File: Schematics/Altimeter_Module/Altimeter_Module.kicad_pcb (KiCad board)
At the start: 4 copper layers, 69.5 x 60 mm, 106 parts, among them J1 Stack Male Edge Connector, J2 Main E-Match, J3 Drogue E-Match, J4 USB_C_Female_USB2_Small, J5 SWD_01x04_Pin, Q1 AO3400A, Q2 AO4406AL, Q3 AO3400A, Q4 AO3400A, Q5 AO4406AL, SW1 SW_STM_RESET, SW2 SW_STM_BOOT_MODE, U1 KX134-1211, U10 ACS70331EOLC, U12 AMS1117-3.3, U2 MS560702BA03-50, U3 W25Q128JVS, U4 LM66100DCKR, U5 LM66100DCKR, U6 STM32F103CBT6, U7 LM66100DCKR, U8 ISO1042BDWVR, U9 MPU-6050, Y1 X322516MMB4SI

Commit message: Design version bump to V1.1
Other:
- board text added: "Oka Rev 1.1 QRET Feb 2025 Joshua Xiang Kennan Bays"
- board text removed: "Oka Rev 1.0 QRET Mar 2024 Joshua Xiang Kennan Bays"
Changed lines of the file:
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@@
     (effects (font (size 1.5 1.5) (thickness 0.3) bold) (justify left bottom mirror))
   )
-  (gr_text "Oka Rev 1.0\nQRET Mar 2024\n\nJoshua Xiang\nKennan Bays" (at 161.25 68.95) (layer "B.SilkS")
+  (gr_text "Oka Rev 1.1\nQRET Feb 2025\n\nJoshua Xiang\nKennan Bays" (at 161.25 68.95) (layer "B.SilkS")
     (effects (font (size 1.5 1.5) (thickness 0.25)) (justify top mirror))
   )

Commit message: Added CP2102 USB bridge
Also bumped version up to V2.0 now that significant hardware changes (e.g. pinout changes) have been made. This breaks firmware backwards compatibility, and thus warrants a major version bump.
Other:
- board text added: "Oka Rev 2.0 QRET Feb 2025 Joshua Xiang Kennan Bays"
- board text removed: "Oka Rev 1.1 QRET Feb 2025 Joshua Xiang Kennan Bays"

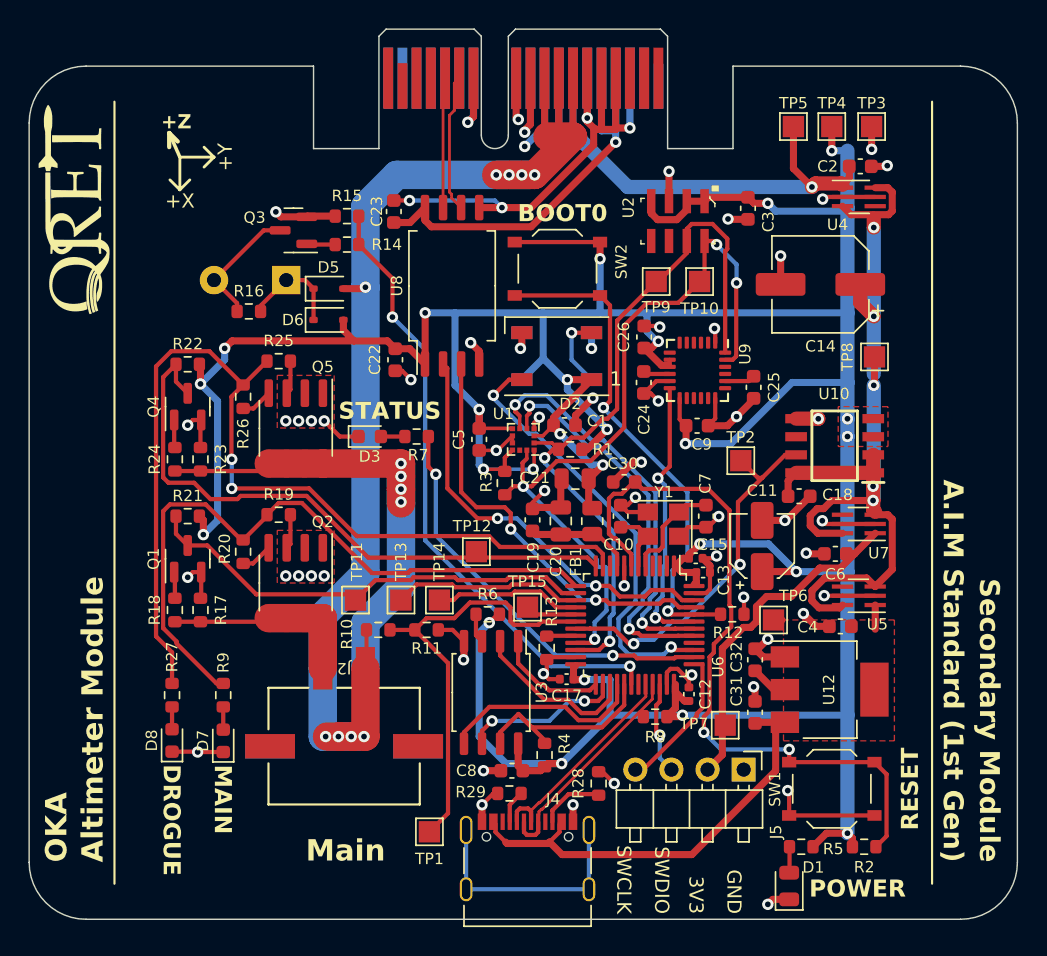
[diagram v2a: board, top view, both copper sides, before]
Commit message: Completed PCB layout
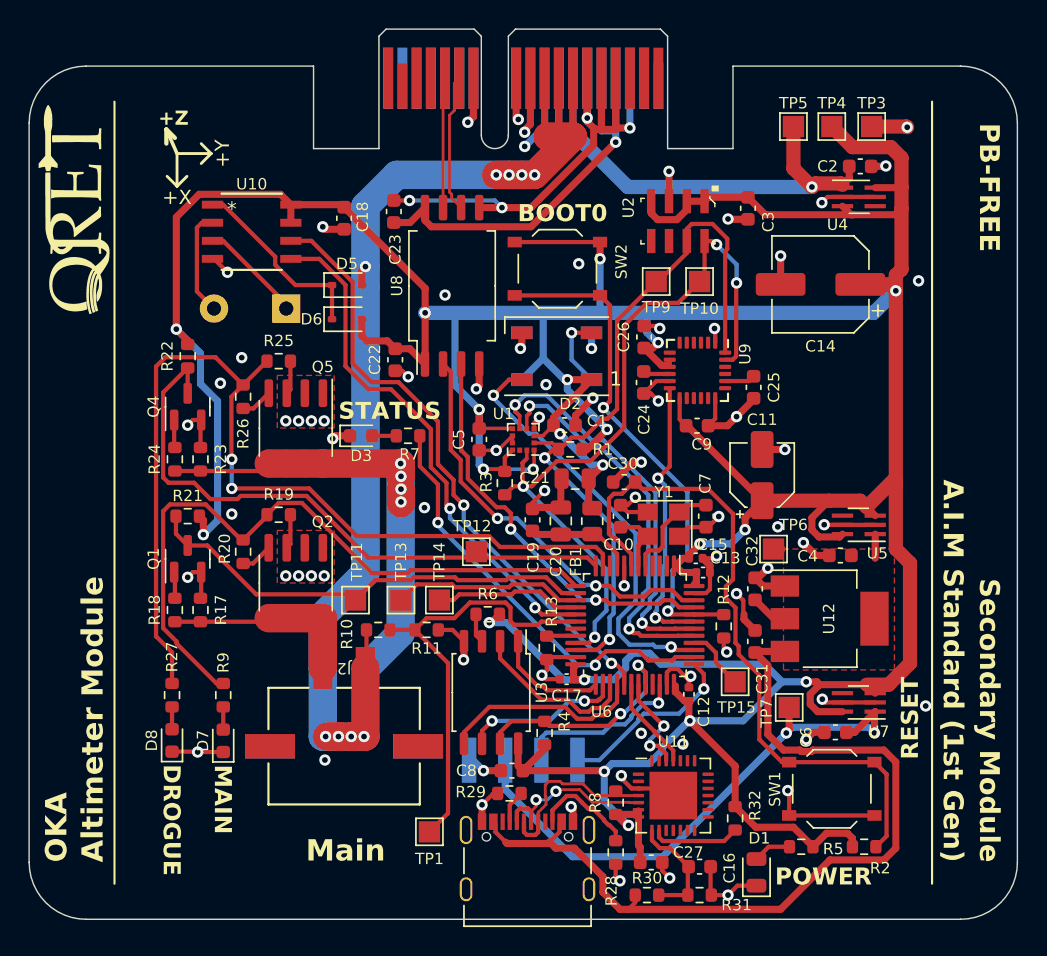
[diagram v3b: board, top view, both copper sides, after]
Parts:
- removed Q3: AO3400A, Package_TO_SOT_SMD:SOT-23
- removed R14: 510R, Resistor_SMD:R_0603_1608Metric
- removed R15: 10k, Resistor_SMD:R_0603_1608Metric
- removed R16: 1k, Resistor_SMD:R_0603_1608Metric
- removed TP2: TP_ISENSE, TestPoint:TestPoint_Pad_1.5x1.5mm
- removed TP8: TP_MUX, TestPoint:TestPoint_Pad_1.5x1.5mm
- added C16: 1uF, Capacitor_SMD:C_0603_1608Metric, F.Cu at (158.7, 113.8)
- added C27: 10uF, Capacitor_SMD:C_0603_1608Metric, F.Cu at (155.3, 113.5)
- added R30: 22k, Resistor_SMD:R_0603_1608Metric, F.Cu at (155.0, 115.8)
- added R31: 47k, Resistor_SMD:R_0603_1608Metric, F.Cu at (158.7, 115.8)
- added R32: 1k, Resistor_SMD:R_0603_1608Metric, F.Cu at (161.2, 110.3)
- added U11: CP2102N-Axx-xQFN28, Package_DFN_QFN:QFN-28-1EP_5x5mm_P0.5mm_EP3.35x3.35mm, F.Cu at (156.8, 108.8)
- BZ1: value PKM13EPYH4000 -> PS1240P02BT
- C18: value 0.1uF -> 100nF
- J5: footprint SWD_Header:SWD_PinHeader_1x04_P2.54mm_Horizontal -> SWD_Header:SWD_PinHeader_1x04_P2.54mm_Horizontal_SMD; moved to B.Cu
- R5: value 1.2k -> 3.3k
- TP15: value TP_PA7 -> TP_PB4
- U1: value KX134-1211 -> QMA6100P
- U10: value ACS70331EOLC -> TPM8837C-SO1R; footprint footprints:SOIC127P600X175-8N -> footprints:SOP-8_TPK
- moved U10 43.7 mm to (127.2, 69.1), turned to 0 degrees
- moved C18 37.5 mm to (133.7, 68.2), turned to -90 degrees
- moved J5 19.3 mm to (142.5, 106.3)
- moved TP15 15.5 mm to (161.2, 100.8)
- moved C6 12.5 mm to (168.2, 104.3)
- moved U7 12.5 mm to (169.9, 102.2)
- moved R8 6.66 mm to (152.8, 109.2), turned to 90 degrees
- moved R28 5.00 mm to (152.8, 112.8), turned to -90 degrees
- moved C31 4.99 mm to (162.6, 97.9)
- moved TP6 4.99 mm to (163.9, 91.4)
- moved C11 4.99 mm to (163.1, 86.2)
- moved C32 4.99 mm to (162.6, 94.2)
- moved C4 4.99 mm to (168.6, 91.9)
- moved U12 4.99 mm to (167.8, 96.3)
- moved U5 4.99 mm to (169.9, 89.7)
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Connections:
- net /USB_5V renamed 5V_RAW
- C14 pad 1: V_MUX -> +3.3V
- C18 pad 1: V_MUX -> +3.3V
- D5 pad 1: Net-(BZ1--) -> Net-(D5-K)
- D6 pad 1: Net-(BZ1--) -> Net-(D5-K)
- TP15 pad 1: Net-(U6-PA7) -> Net-(U6-PB4)
- U10 pad 1: V_MUX -> Net-(D5-K)
- U10 pad 2: V_MUX -> Net-(BZ1-+)
- U10 pad 3: +3.3V -> Net-(BZ1--)
- U10 pad 4: +3.3V -> GND
- U10 pad 5: GND -> BUZZER_B
- U10 pad 6: unconnected-(U10-NC-Pad6) -> BUZZER_A
- U10 pad 7: CURR_SENSE -> +3.3V
- U10 pad 8: V_MUX -> +3.3V
- U4 pad 3: V_MUX -> +3.3V
- U4 pad 6: V_MUX -> +3.3V
- U5 pad 3: V_MUX -> +3.3V
- U5 pad 6: V_MUX -> +3.3V
- U6 pad 17: Net-(U6-PA7) -> BUZZER_B
- U6 pad 19: CURR_SENSE -> unconnected-(U6-PB1-Pad19)
- U6 pad 29: RESET_FL -> BUZZER_A
- U6 pad 30: BUZZER -> USB_TX
- U6 pad 31: unconnected-(U6-PA10-Pad31) -> USB_RX
- U6 pad 32: USB_D- -> RESET_FL
- U6 pad 33: USB_D+ -> unconnected-(U6-PA12-Pad33)
- U6 pad 40: unconnected-(U6-PB4-Pad40) -> Net-(U6-PB4)
- U7 pad 3: V_MUX -> +3.3V
- U7 pad 6: V_MUX -> +3.3V
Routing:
- net +3.3V: track 297.6 -> 368.3 mm, vias 25 -> 21
- net V_MUX: track 64.2 -> 0.00 mm, vias 5 -> 0
- net BUZZER: track 44.1 -> 0.00 mm, vias 2 -> 0
- net BUZZER_A: track 0.00 -> 43.2 mm, vias 0 -> 2
- net BUZZER_B: track 0.00 -> 36.8 mm, vias 0 -> 2
- net 5V_RAW: track 30.7 -> 60.4 mm
- net CURR_SENSE: track 26.2 -> 0.00 mm, vias 2 -> 0
- net unconnected-(J4-SHIELD-PadS1): track 17.0 -> 0.00 mm
- net V_SWD: track 24.3 -> 40.0 mm, vias 0 -> 2
- net Net-(D5-K): track 0.00 -> 13.5 mm
- net Net-(U11-VBUS): track 0.00 -> 8.11 mm
- net USB_RX: track 0.00 -> 7.34 mm, vias 0 -> 2
- net GND: track 146.5 -> 153.5 mm, vias 57 -> 73
- net USB_TX: track 0.00 -> 6.60 mm
- net Net-(U11-~{RST}): track 0.00 -> 6.26 mm
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- removed copper zone on F.Cu, net +3.3V
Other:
- board text added: "PB-FREE"

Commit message: Adjusted PCB layout
- Moved E-Match connectors forward 4mm
- Added polarity silkscreen to E-Match connectors
- Adjusted attribution silkscreen
- Added testpoint silkscreen labels
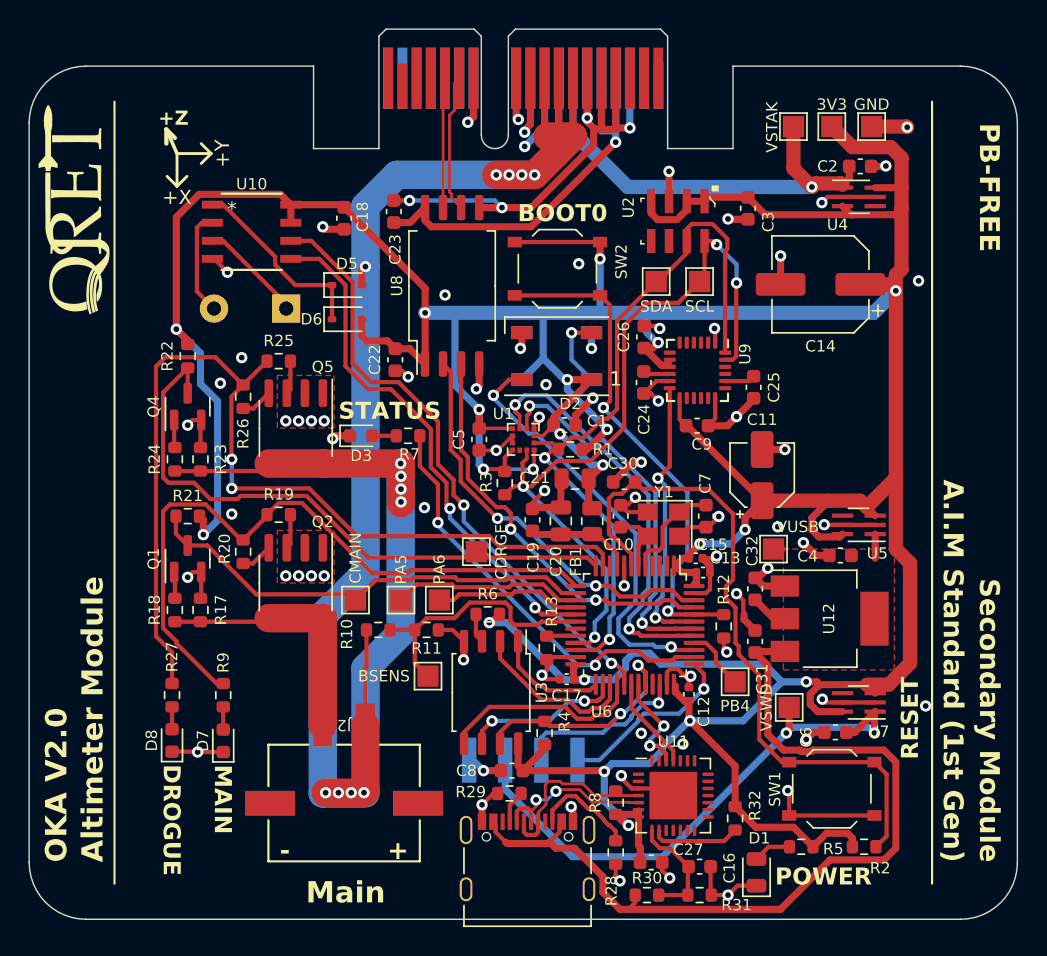
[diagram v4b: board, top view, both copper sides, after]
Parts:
- Q2, Q5: value AO4406AL -> AO4406A
- TP1: value TP_BSENSE -> BSENS
- TP10: value TP_SCL -> SCL
- TP11: value TP_CMAIN -> CMAIN
- TP12: value TP_CDRGE -> CDRGE
- TP13: value TP_PA5 -> PA5
- TP14: value TP_PA6 -> PA6
- TP15: value TP_PB4 -> PB4
- TP3: value TP_GND -> GND
- TP4: value TP_3V3 -> 3V3
- TP5: value TP_VSTACK -> VSTAK
- TP6: value TP_VUSB -> VUSB
- TP7: value TP_VSWD -> VSWD
- TP9: value TP_SDA -> SDA
- moved TP1 11.0 mm to (139.6, 100.3)
- moved J2 4.00 mm to (135.2, 103.8)
- moved J3 4.00 mm to (132.2, 103.8)
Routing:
- net BATT_SENSE: track 30.9 -> 18.8 mm
- net +BATT: track 86.2 -> 94.3 mm
- net Net-(J2-Pad2): track 14.0 -> 18.0 mm
- net Net-(J3-Pad2): track 33.4 -> 37.4 mm
- net GND: vias 73 -> 72
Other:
- board text added: "- +"
- board text added: "OKA V2.0"
- board text added: "Oka Rev 2.0 QRET Mar 2025 Joshua Xiang Kennan Bays"
- board text removed: "OKA"
- board text removed: "Oka Rev 2.0 QRET Feb 2025 Joshua Xiang Kennan Bays"

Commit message: Final adjustments + improved QMA6100 clearance
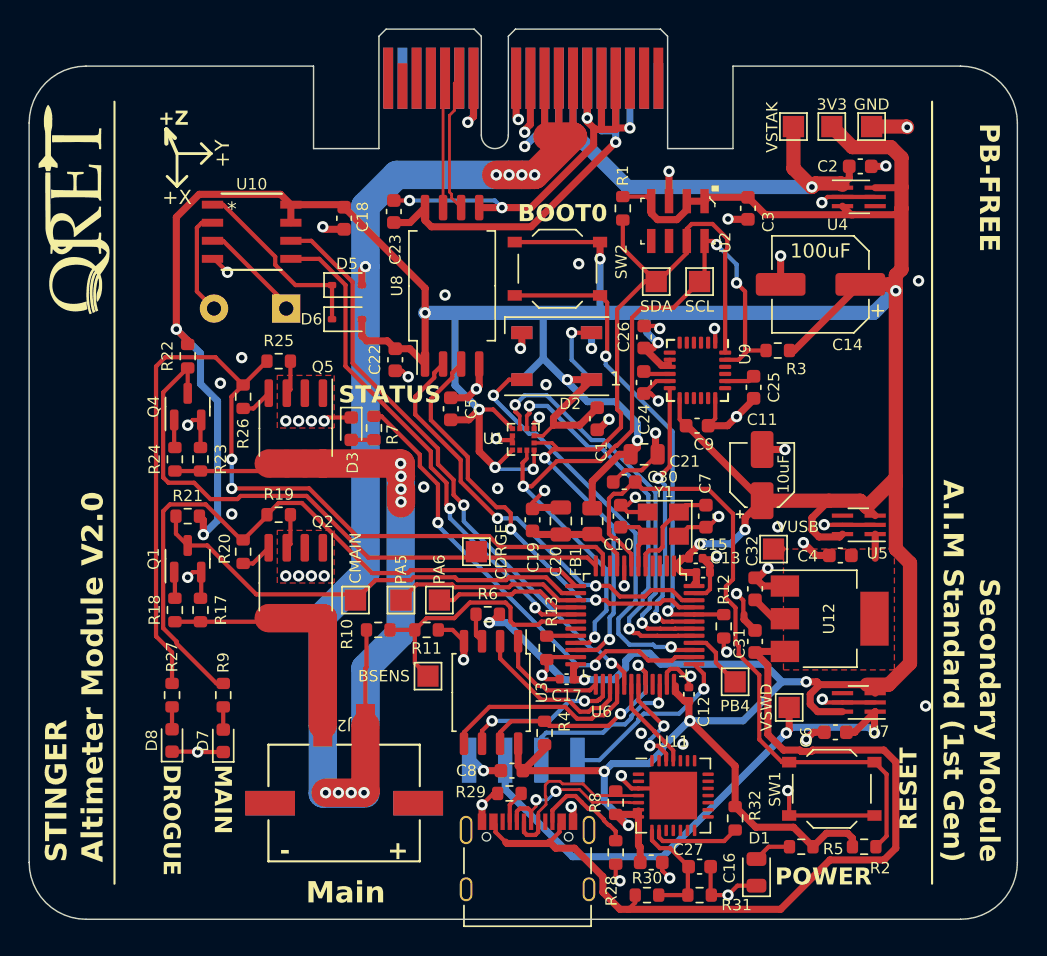
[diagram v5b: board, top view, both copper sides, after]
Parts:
- moved R3 21.3 mm to (164.2, 77.5), turned to 180 degrees
- moved R1 17.3 mm to (153.3, 67.5), turned to 90 degrees
- moved C21 5.14 mm to (154.8, 84.8), turned to 0 degrees
- moved C5 2.94 mm to (141.2, 81.5), turned to -90 degrees
- moved R7 2.46 mm to (135.8, 82.9), turned to 90 degrees
- moved C1 2.34 mm to (151.5, 82.2), turned to -90 degrees
- moved D3 0.86 mm to (134.2, 83.0), turned to -90 degrees
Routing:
- net +3.3V: track 368.3 -> 379.8 mm, vias 21 -> 19
- net SDA: track 52.0 -> 59.0 mm
- net DB_LED: track 29.8 -> 32.9 mm
- net CAN_RX: track 28.8 -> 30.5 mm
- net CAN_TX: track 28.9 -> 30.5 mm
- net SCL: track 54.4 -> 55.7 mm
- net BOOT0: track 35.5 -> 34.3 mm
- net BUZZER_A: track 43.2 -> 42.1 mm
- net BUZZER_B: track 36.8 -> 35.9 mm
- net GND: track 153.5 -> 154.2 mm
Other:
- board text added: "Altimeter Module V2.0"
- board text added: "Altimeter Rev 2.0 QRET Mar 2025 Joshua Xiang Kennan Bays"
- board text added: "STINGER"
- board text removed: "Altimeter Module"
- board text removed: "OKA V2.0"
- board text removed: "Oka Rev 2.0 QRET Mar 2025 Joshua Xiang Kennan Bays"

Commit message: Silkscreen tweak
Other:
- board text added: "Altimeter Module Rev 2.0 QRET Mar 2025 Joshua Xiang Kennan Bays"
- board text removed: "Altimeter Rev 2.0 QRET Mar 2025 Joshua Xiang Kennan Bays"
